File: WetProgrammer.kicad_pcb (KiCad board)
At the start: 2 copper layers, 48 x 25 mm, 40 parts, among them J1 USB_B_Micro, J2 AVR-ISP-6, J3 Conn_01x03_Male, SW1 SW_SPDT, SW2 SW_SPDT, U1 ATmega32U4-AU, U2 TLV1117-33, Y1 16MHz

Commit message: at some point i will be good at boards
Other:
- board text added: "Rev 1.0, Sep 2021 github.com/timChase98/ WetAvrProgrammer"
- board text removed: "Rev 1.0, Sep 2021 github.com/timChase98/WetAvrProgrammer"
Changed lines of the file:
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@@
     (effects (font (size 1 1) (thickness 0.15)))
   )
-  (gr_text "Rev 1.0,  Sep 2021\ngithub.com/timChase98/WetAvrProgrammer\n" (at 3.6068 -2.6924) (layer B.SilkS)
-    (effects (font (size 1 1) (thickness 0.1524)) (justify right mirror))
+  (gr_text "Rev 1.0,  Sep 2021\ngithub.com/timChase98/\nWetAvrProgrammer\n" (at 41 -6.75) (layer B.SilkS)
+    (effects (font (size 1 1) (thickness 0.1524)) (justify left mirror))
   )
   (gr_text "Target\nPower\n" (at 44.831 -19.2405) (layer F.SilkS)
@@
     (polygon
       (pts
-        (xy 48.768 1) (xy -1 1) (xy -1 -26) (xy 49 -26)
+        (xy 49 1) (xy -1 1) (xy -1 -26) (xy 49 -26)
       )
     )

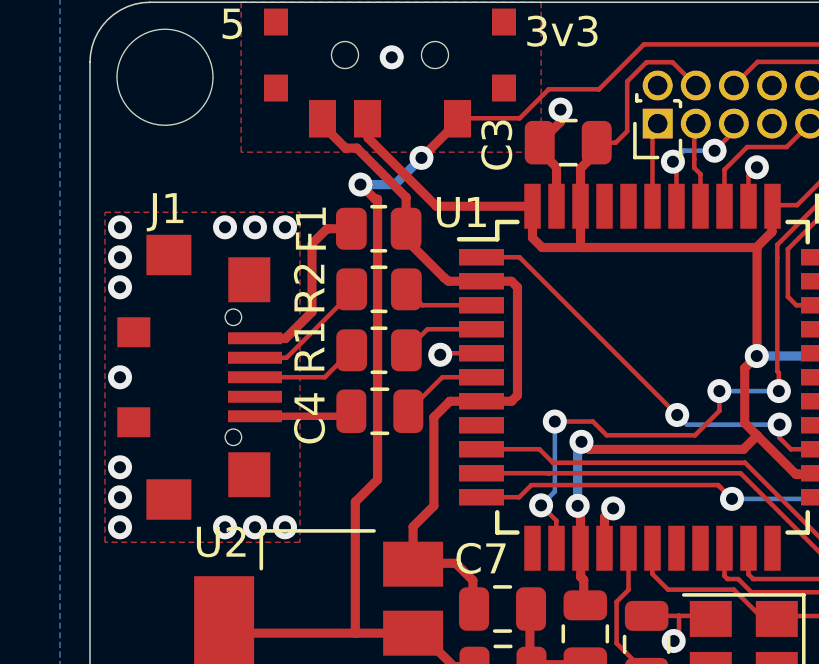
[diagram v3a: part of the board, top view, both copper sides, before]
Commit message: Fixed Switch Labels
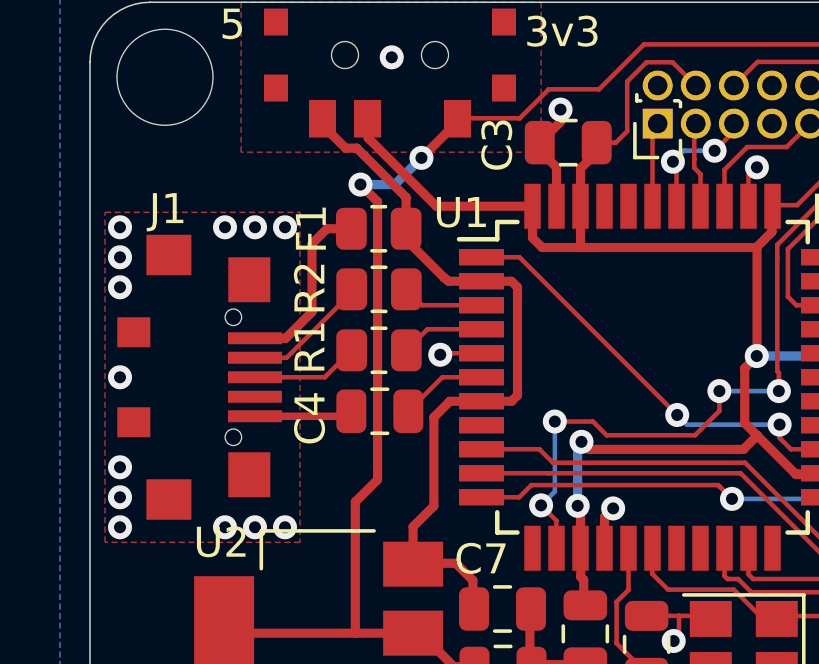
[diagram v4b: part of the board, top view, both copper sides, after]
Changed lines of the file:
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@@
     (thickness 1.6)
     (drawings 16)
-    (tracks 368)
+    (tracks 367)
     (zones 0)
     (modules 40)
@@
   (segment (start 12.7635 -4.826) (end 12.7635 -5.7277) (width 0.3048) (layer F.Cu) (net 4))
   (segment (start 4.572 -3.9695) (end 4.5085 -4.033) (width 0.3048) (layer F.Cu) (net 5))
-  (segment (start 8.8445 -3.9695) (end 8.8445 -8.3445) (width 0.3048) (layer F.Cu) (net 5))
   (segment (start 10.77 -3.9695) (end 8.8445 -3.9695) (width 0.3048) (layer F.Cu) (net 5))
   (segment (start 8.8445 -3.9695) (end 4.572 -3.9695) (width 0.3048) (layer F.Cu) (net 5))
-  (segment (start 9.58641 -9.08641) (end 9.58641 -18.43641) (width 0.3048) (layer F.Cu) (net 5))
-  (segment (start 8.8445 -8.3445) (end 9.58641 -9.08641) (width 0.3048) (layer F.Cu) (net 5))
   (via (at 9.017 -18.923) (size 0.8) (drill 0.4) (layers F.Cu B.Cu) (net 5))
-  (segment (start 9.50359 -18.43641) (end 9.017 -18.923) (width 0.3048) (layer F.Cu) (net 5))
-  (segment (start 9.58641 -18.43641) (end 9.50359 -18.43641) (width 0.3048) (layer F.Cu) (net 5))
   (segment (start 10.16 -18.923) (end 11.049 -19.812) (width 0.3048) (layer B.Cu) (net 5))
   (segment (start 9.017 -18.923) (end 10.16 -18.923) (width 0.3048) (layer B.Cu) (net 5))
@@
   (segment (start 31.8747 -20.7541) (end 29.03319 -23.59561) (width 0.1524) (layer F.Cu) (net 5))
   (segment (start 31.8747 -18.0848) (end 31.8747 -20.7541) (width 0.1524) (layer F.Cu) (net 5))
+  (segment (start 9.58641 -18.35359) (end 9.017 -18.923) (width 0.3048) (layer F.Cu) (net 5))
+  (segment (start 9.58641 -9.08641) (end 9.58641 -18.35359) (width 0.3048) (layer F.Cu) (net 5))
+  (segment (start 8.8445 -8.3445) (end 9.58641 -9.08641) (width 0.3048) (layer F.Cu) (net 5))
+  (segment (start 8.8445 -3.9695) (end 8.8445 -8.3445) (width 0.3048) (layer F.Cu) (net 5))
   (segment (start 28.2956 -18.0848) (end 29.8704 -18.0848) (width 0.1524) (layer F.Cu) (net 6))
   (segment (start 29.8704 -18.0848) (end 30.0228 -18.0848) (width 0.1524) (layer F.Cu) (net 6))
